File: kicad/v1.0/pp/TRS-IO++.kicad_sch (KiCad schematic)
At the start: 102 parts, among them J1 TRS-80 M3 Pin Header, J10 Cassette Input, J11 Mini-DIN-6, J12 USB_B_Micro, J13 UART, J2 TRS-80 M1 Pin Header, J3 TRS-80 M3 Edge Connector, J4 TRS-80 M1 Edge Connector, J5 Conn_02x06_Odd_Even, J6 Cassette Output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

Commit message: Custom TRS-IO++ PCB (incomplete, no video)
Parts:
- removed C16: 0.1uF, Capacitor_SMD:C_0805_2012Metric_Pad1.18x1.45mm_HandSolder, symbol Device:C
- removed D1: LED_RKBG, LED_THT:LED_D5.0mm-4_RGB, symbol Device:LED_RKBG
- removed H5, H6: MountingHole, PocketTRS_Connectors:Alignment_Hole_2.6mm, symbol Mechanical:MountingHole
- removed J1: TRS-80 M3 Pin Header, Connector_PinHeader_2.54mm:PinHeader_2x25_P2.54mm_Vertical, symbol Connector_Generic:Conn_02x25_Odd_Even
- removed J10: Cassette Input, PocketTRS_Connectors:Jack_3.5mm_CUI_SJ1-3535NG_Horizontal_CircularHoles, symbol Connector:AudioJack3
- removed J11: Mini-DIN-6, PocketTRS_Connectors:minidin_6_ps2_pcb_mount, symbol Connector:Mini-DIN-6
- removed J2: TRS-80 M1 Pin Header, Connector_PinHeader_2.54mm:PinHeader_2x20_P2.54mm_Vertical, symbol Connector_Generic:Conn_02x20_Odd_Even
- removed J4: TRS-80 M1 Edge Connector, trs-io-m1:TRSEDGE, symbol Connector_Generic:Conn_02x20_Odd_Even
- removed J9: SD_Card, PocketTRS_Connectors:TFP09-2-12B, symbol SDCard:SD_Card
- removed R16, R18: 10K, Resistor_SMD:R_0805_2012Metric_Pad1.20x1.40mm_HandSolder, symbol Device:R
- removed R31, R32: 2K, Resistor_SMD:R_0805_2012Metric_Pad1.20x1.40mm_HandSolder, symbol Device:R
- removed SW1: ESP_RESET, Button_Switch_THT:SW_PUSH_6mm, symbol Switch:SW_Push
- removed SW2: PTRS_RESET, Button_Switch_THT:SW_PUSH_6mm, symbol Switch:SW_Push
- removed SW4: TRS_IO_STATUS, Button_Switch_THT:SW_PUSH_6mm, symbol Switch:SW_Push
- removed U4: 74LVC245, trs-io-m3:SSOP-20_5.3x7.2mm_P0.65mm_slim, symbol 74xx:74HC245
- added J1: Conn_02x06_Odd_Even, Connector_PinSocket_2.54mm:PinSocket_2x06_P2.54mm_Vertical, symbol Connector_Generic:Conn_02x06_Odd_Even
- added J2: Conn_01x16, Connector_PinHeader_2.54mm:PinHeader_1x16_P2.54mm_Vertical, symbol Connector_Generic:Conn_01x16
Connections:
- net +3V3: now also J1.11 (Pin_11), J1.12 (Pin_12), J2.2 (Pin_2)
- net CD_SD: now also J2.5 (Pin_5)
- net CS_SD: now also J2.7 (Pin_7)
- net D0: now also RN1.2 (R1); no longer RN1.3 (R2)
- net D1: now also RN1.3 (R2); no longer RN1.7 (R6)
- net D2: now also RN1.4 (R3); no longer RN1.2 (R1)
- net D4: now also RN1.6 (R5); no longer RN1.9 (R8)
- net D5: now also RN1.7 (R6); no longer RN1.4 (R3)
- net D6: now also RN1.8 (R7); no longer RN1.6 (R5)
- net D7: now also RN1.9 (R8); no longer RN1.8 (R7)
- net ESP_RESET: now also J2.10 (Pin_10)
- net GND: now also J1.10 (Pin_10), J1.9 (Pin_9), J2.1 (Pin_1)
- net ID0: now also J2.9 (Pin_9)
- net IN_N: now also U3.9 (A7); no longer U3.2 (A0)
- net IOREQ_N: now also U3.5 (A3); no longer U3.7 (A5)
- net M1_N: now also U3.6 (A4); no longer U3.8 (A6)
- net OUT_N: now also U3.8 (A6); no longer U3.5 (A3)
- net RAS_N: now also U3.4 (A2); no longer U3.6 (A4)
- net RD_N: now also U3.2 (A0); no longer U3.3 (A1)
- net RESET_N: now also U3.7 (A5); no longer U3.9 (A7)
- net WR_N: now also U3.3 (A1); no longer U3.4 (A2)
- net _IN_N: now also Conn1.53 (T11), U3.11 (B7); no longer Conn1.33 (T7), U3.18 (B0)
- net _IOREQ_N: now also Conn1.41 (P8), U3.15 (B3); no longer Conn1.47 (P9), U3.13 (B5)
- net _M1_N: now also Conn1.45 (T9), U3.14 (B4); no longer Conn1.51 (P11), U3.12 (B6)
- net _OUT_N: now also Conn1.51 (P11), U3.12 (B6); no longer Conn1.41 (P8), U3.15 (B3)
- net _RAS_N: now also Conn1.39 (T8), U3.16 (B2); no longer Conn1.45 (T9), U3.14 (B4)
- net _RD_N: now also Conn1.33 (T7), U3.18 (B0); no longer Conn1.35 (R8), U3.17 (B1)
- net _RESET_N: now also Conn1.47 (P9), U3.13 (B5); no longer Conn1.53 (T11), U3.11 (B7)
- net _WR_N: now also Conn1.35 (R8), U3.17 (B1); no longer Conn1.39 (T8), U3.16 (B2)
- net IF_LED_BLUE: now reaches R3.2
- net IF_LED_BLUE: now also J2.13 (Pin_13)
- net IF_CASS_IN: now reaches C14.1
- net IF_CASS_IN: now also J2.11 (Pin_11)
- net IF_LED_RED: now reaches R1.2
- net IF_LED_RED: now also J2.12 (Pin_12)
- net IF_LED_GREEN: now reaches R2.2
- net IF_LED_GREEN: now also J2.14 (Pin_14)
- net MISO renamed IF_SD_MISO
- net IF_SD_MISO: now also J2.3 (Pin_3)
- net MOSI renamed IF_SD_MOSI
- net IF_SD_MOSI: now also J2.6 (Pin_6)
- net PMOD_IO1 renamed PMOD1_IO1
- net PMOD_IO2 renamed PMOD1_IO2
- net PMOD_IO3 renamed PMOD1_IO3
- net PMOD_IO4 renamed PMOD1_IO4
- net PMOD_IO5 renamed PMOD1_IO5
- net PMOD_IO6 renamed PMOD1_IO6
- net PMOD_IO7 renamed PMOD1_IO7
- net PMOD_IO8 renamed PMOD1_IO8
- net PS2_CLK: no longer names the net of U1.9 (IO33)
- net PS2_DATA: no longer names the net of U1.8 (IO32)
- net RXD0 renamed IF_TXD0
- net IF_TXD0: now also J2.16 (Pin_16)
- net SCK renamed IF_SD_SCK
- net IF_SD_SCK: now also J2.4 (Pin_4)
- net STATUS renamed IF_BTN_TRSIO_STATUS
- net IF_BTN_TRSIO_STATUS: now also J2.8 (Pin_8)
- net TXD0 renamed IF_RXD0
- net IF_RXD0: now also J2.15 (Pin_15)
- net _A10 renamed PMOD2_IO4
- net PMOD2_IO4: now also J1.7 (Pin_7)
- net _A11 renamed PMOD2_IO5
- net PMOD2_IO5: now also J1.2 (Pin_2)
- net _A12 renamed PMOD2_IO7
- net PMOD2_IO7: now also J1.6 (Pin_6)
- net _A13 renamed PMOD2_IO3
- net PMOD2_IO3: now also J1.5 (Pin_5)
- net _A14 renamed PMOD2_IO2
- net PMOD2_IO2: now also J1.3 (Pin_3)
- net _A15 renamed PMOD2_IO6
- net PMOD2_IO6: now also J1.4 (Pin_4)
- net _A8 renamed PMOD2_IO1
- net PMOD2_IO1: now also J1.1 (Pin_1)
- net _A9 renamed PMOD2_IO8
- net PMOD2_IO8: now also J1.8 (Pin_8)
- no-connect marks 14 -> 11
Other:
- note removed: "Note: the pin numbers do NOT correspond with the pinout of the M1 expansion interface because of the non-standard numbering used for the M1."
- moved on the sheet: J3, R14, R30

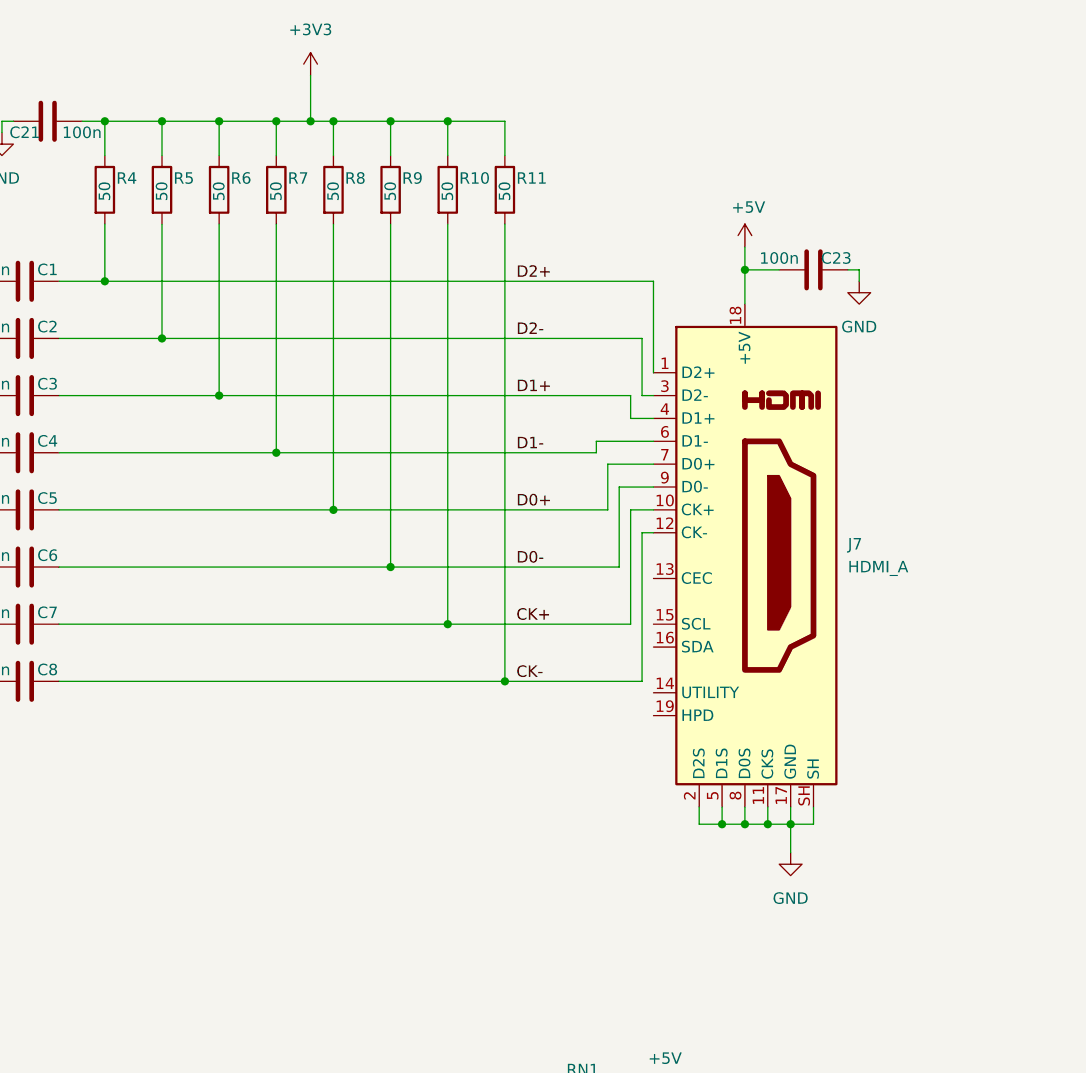
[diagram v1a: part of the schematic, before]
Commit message: Changed HDMI connector to 10 pin header.
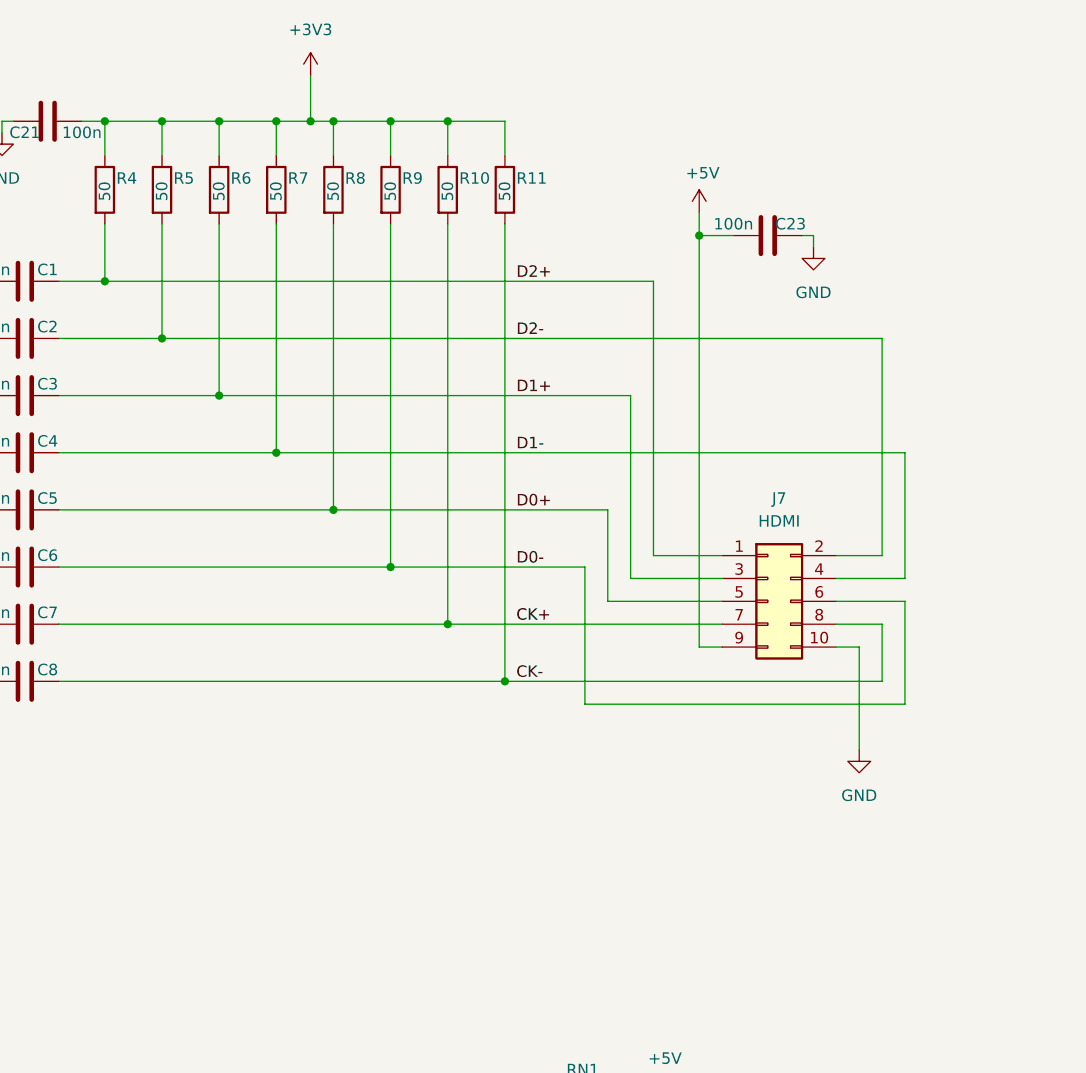
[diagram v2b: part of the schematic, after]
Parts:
- removed J7: HDMI_A, trs-io-m1:HDMI_A_Molex_208658-1001_Horizontal, symbol Connector:HDMI_A
- added J7: HDMI, Connector_PinHeader_1.27mm:PinHeader_2x05_P1.27mm_Vertical, symbol Connector_Generic:Conn_02x05_Odd_Even
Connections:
- net +5V: now also J7.9 (Pin_9)
- net CK+: now also J7.7 (Pin_7)
- net CK-: now also J7.8 (Pin_8)
- net D0+: now also J7.5 (Pin_5)
- net D0-: now also J7.6 (Pin_6)
- net D1+: now also J7.3 (Pin_3)
- net D1-: now also J7.4 (Pin_4)
- net D2+: now also J7.1 (Pin_1)
- net D2-: now also J7.2 (Pin_2)
- net GND: now also J7.10 (Pin_10)
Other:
- moved on the sheet: C23

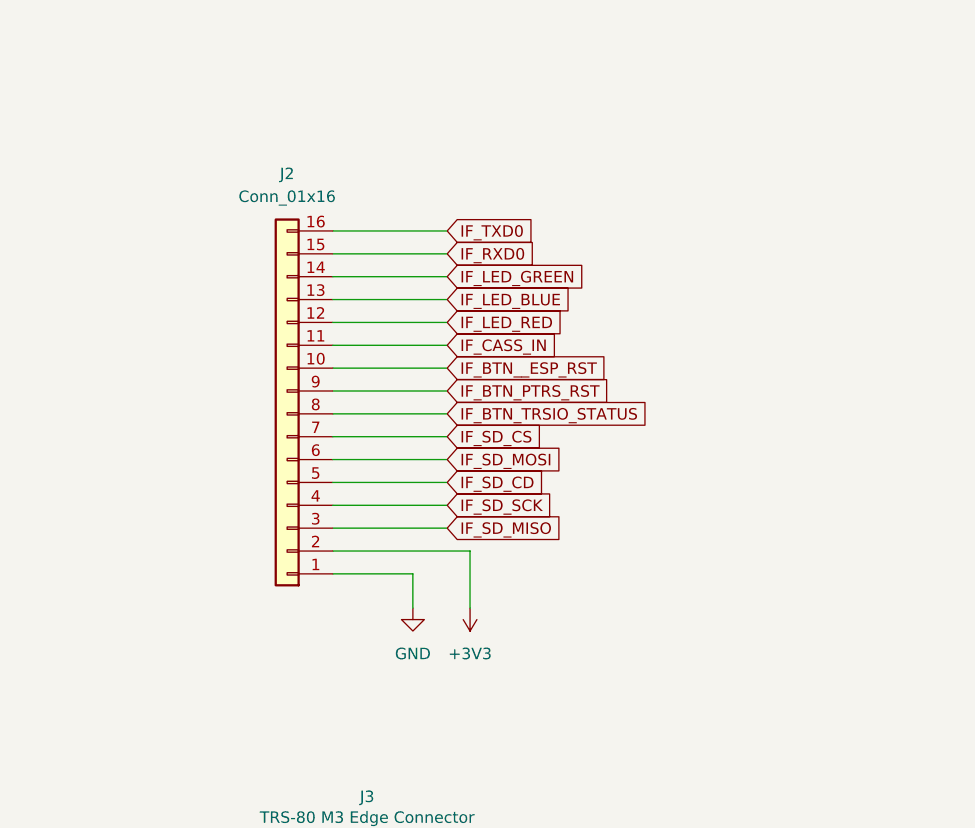
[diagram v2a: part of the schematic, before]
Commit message: Updates to KiCad schematics/layout
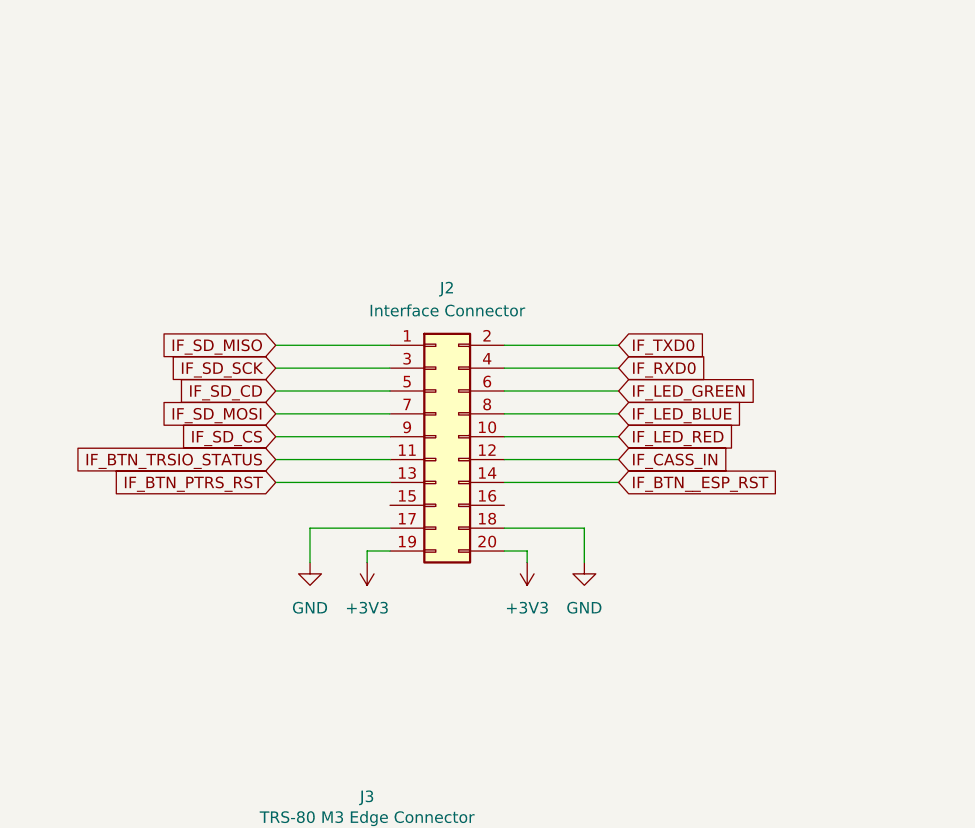
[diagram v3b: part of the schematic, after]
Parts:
- removed J2: Conn_01x16, Connector_PinHeader_2.54mm:PinHeader_1x16_P2.54mm_Vertical, symbol Connector_Generic:Conn_01x16
- added J2: Interface Connector, Connector_PinHeader_2.54mm:PinHeader_2x10_P2.54mm_Vertical, symbol Connector_Generic:Conn_02x10_Odd_Even
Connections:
- net +3V3: now also J2.19 (Pin_19), J2.20 (Pin_20)
- net CD_SD: now also J2.5 (Pin_5)
- net CS_SD: now also J2.9 (Pin_9)
- net ESP_RESET: now also J2.14 (Pin_14)
- net GND: now also J2.17 (Pin_17), J2.18 (Pin_18)
- net ID0: now also J2.13 (Pin_13)
- net IF_BTN_TRSIO_STATUS: now also J2.11 (Pin_11)
- net IF_CASS_IN: now also J2.12 (Pin_12)
- net IF_LED_BLUE: now also J2.8 (Pin_8)
- net IF_LED_GREEN: now also J2.6 (Pin_6)
- net IF_LED_RED: now also J2.10 (Pin_10)
- net IF_RXD0: now also J2.4 (Pin_4)
- net IF_SD_MISO: now also J2.1 (Pin_1)
- net IF_SD_MOSI: now also J2.7 (Pin_7)
- net IF_SD_SCK: now also J2.3 (Pin_3)
- net IF_TXD0: now also J2.2 (Pin_2)
